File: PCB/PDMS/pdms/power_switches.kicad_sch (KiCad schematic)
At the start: 8 parts

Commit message: PCB clean up
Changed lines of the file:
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@@
-    (stroke (width 0) (type default) (color 0 0 0 0))
-  )
-  (bus_entry (at 213.36 86.36) (size 2.54 -2.54)
     (stroke (width 0) (type default) (color 0 0 0 0))
   )
@@
     (stroke (width 0) (type default) (color 0 0 0 0))
   )
-  (bus_entry (at 213.36 147.32) (size 2.54 -2.54)
+  (bus_entry (at 213.36 153.035) (size 2.54 -2.54)
     (stroke (width 0) (type default) (color 0 0 0 0))
   )
@@
     (stroke (width 0) (type default) (color 0 0 0 0))
   )
-  (bus_entry (at 215.9 86.36) (size 2.54 -2.54)
-    (stroke (width 0) (type default) (color 0 0 0 0))
-  )
   (bus_entry (at 48.26 116.84) (size 2.54 -2.54)
     (stroke (width 0) (type default) (color 0 0 0 0))
@@
     (stroke (width 0) (type default) (color 0 0 0 0))
   )
+  (bus_entry (at 213.36 92.075) (size 2.54 -2.54)
+    (stroke (width 0) (type default) (color 0 0 0 0))
+  )
   (bus_entry (at 185.42 121.92) (size 2.54 2.54)
     (stroke (width 0) (type default) (color 0 0 0 0))
@@
     (stroke (width 0) (type default) (color 0 0 0 0))
   )
-  (bus_entry (at 210.82 147.32) (size 2.54 -2.54)
-    (stroke (width 0) (type default) (color 0 0 0 0))
-  )
-  (bus_entry (at 210.82 86.36) (size 2.54 -2.54)
+  (bus_entry (at 210.82 153.035) (size 2.54 -2.54)
     (stroke (width 0) (type default) (color 0 0 0 0))
   )
@@
     (stroke (width 0) (type default) (color 0 0 0 0))
   )
-  (bus_entry (at 215.9 147.32) (size 2.54 -2.54)
+  (bus_entry (at 210.82 92.075) (size 2.54 -2.54)
+    (stroke (width 0) (type default) (color 0 0 0 0))
+  )
+  (bus_entry (at 215.9 92.075) (size 2.54 -2.54)
+    (stroke (width 0) (type default) (color 0 0 0 0))
+  )
+  (bus_entry (at 215.9 153.035) (size 2.54 -2.54)
     (stroke (width 0) (type default) (color 0 0 0 0))
   )
@@
     (stroke (width 0) (type default) (color 0 0 0 0))
   )
-  (bus (pts (xy 205.74 149.86) (xy 205.74 147.32))
+  (bus (pts (xy 205.74 155.575) (xy 205.74 153.035))
     (stroke (width 0) (type default) (color 0 0 0 0))
   )
@@
     (stroke (width 0) (type default) (color 0 0 0 0))
   )
+  (bus (pts (xy 210.82 92.075) (xy 213.36 92.075))
+    (stroke (width 0) (type default) (color 0 0 0 0))
+  )
   (wire (pts (xy 88.9 68.58) (xy 90.805 68.58))
     (stroke (width 0) (type default) (color 0 0 0 0))
@@
     (stroke (width 0) (type default) (color 0 0 0 0))
   )
-  (bus (pts (xy 213.36 147.32) (xy 215.9 147.32))
-    (stroke (width 0) (type default) (color 0 0 0 0))
-  )
-  (wire (pts (xy 218.44 78.74) (xy 218.44 83.82))
+  (bus (pts (xy 213.36 153.035) (xy 215.9 153.035))
     (stroke (width 0) (type default) (color 0 0 0 0))
   )
@@
     (stroke (width 0) (type default) (color 0 0 0 0))
   )
+  (wire (pts (xy 218.44 78.74) (xy 218.44 89.535))
+    (stroke (width 0) (type default) (color 0 0 0 0))
+  )
   (bus (pts (xy 114.3 88.9) (xy 114.3 111.76))
     (stroke (width 0) (type default) (color 0 0 0 0))
@@
     (stroke (width 0) (type default) (color 0 0 0 0))
   )
-  (bus (pts (xy 210.82 147.32) (xy 213.36 147.32))
+  (bus (pts (xy 210.82 153.035) (xy 213.36 153.035))
     (stroke (width 0) (type default) (color 0 0 0 0))
   )
@@
     (stroke (width 0) (type default) (color 0 0 0 0))
   )
-  (wire (pts (xy 218.44 139.7) (xy 218.44 144.78))
+  (wire (pts (xy 218.44 139.7) (xy 218.44 150.495))
     (stroke (width 0) (type default) (color 0 0 0 0))
   )
@@
     (stroke (width 0) (type default) (color 0 0 0 0))
   )
-  (wire (pts (xy 213.36 78.74) (xy 213.36 83.82))
+  (wire (pts (xy 215.9 78.74) (xy 215.9 89.535))
     (stroke (width 0) (type default) (color 0 0 0 0))
   )
@@
     (stroke (width 0) (type default) (color 0 0 0 0))
   )
-  (bus (pts (xy 215.9 86.36) (xy 218.44 86.36))
-    (stroke (width 0) (type default) (color 0 0 0 0))
-  )
   (bus (pts (xy 185.42 60.96) (xy 185.42 63.5))
     (stroke (width 0) (type default) (color 0 0 0 0))
@@
     (stroke (width 0) (type default) (color 0 0 0 0))
   )
-  (wire (pts (xy 213.36 139.7) (xy 213.36 144.78))
+  (wire (pts (xy 213.36 139.7) (xy 213.36 150.495))
     (stroke (width 0) (type default) (color 0 0 0 0))
   )
@@
     (stroke (width 0) (type default) (color 0 0 0 0))
   )
+  (wire (pts (xy 213.36 78.74) (xy 213.36 89.535))
+    (stroke (width 0) (type default) (color 0 0 0 0))
+  )
   (wire (pts (xy 116.84 66.04) (xy 127 66.04))
     (stroke (width 0) (type default) (color 0 0 0 0))
@@
     (stroke (width 0) (type default) (color 0 0 0 0))
   )
-  (wire (pts (xy 215.9 78.74) (xy 215.9 83.82))
-    (stroke (width 0) (type default) (color 0 0 0 0))
-  )
   (wire (pts (xy 187.96 60.96) (xy 203.2 60.96))
     (stroke (width 0) (type default) (color 0 0 0 0))
@@
     (stroke (width 0) (type default) (color 0 0 0 0))
   )
-  (bus (pts (xy 205.74 88.9) (xy 205.74 86.36))
-    (stroke (width 0) (type default) (color 0 0 0 0))
-  )
   (bus (pts (xy 109.22 73.66) (xy 109.22 93.98))
     (stroke (width 0) (type default) (color 0 0 0 0))
@@
     (stroke (width 0) (type default) (color 0 0 0 0))
   )
+  (bus (pts (xy 205.74 94.615) (xy 205.74 92.075))
+    (stroke (width 0) (type default) (color 0 0 0 0))
+  )
   (wire (pts (xy 111.76 71.12) (xy 127 71.12))
     (stroke (width 0) (type default) (color 0 0 0 0))
   )
-  (bus (pts (xy 213.36 86.36) (xy 215.9 86.36))
-    (stroke (width 0) (type default) (color 0 0 0 0))
-  )
   (bus (pts (xy 43.18 45.72) (xy 53.34 45.72))
     (stroke (width 0) (type default) (color 0 0 0 0))
@@
     (stroke (width 0) (type default) (color 0 0 0 0))
   )
+  (bus (pts (xy 215.9 92.075) (xy 218.44 92.075))
+    (stroke (width 0) (type default) (color 0 0 0 0))
+  )
   (wire (pts (xy 152.4 68.58) (xy 154.305 68.58))
     (stroke (width 0) (type default) (color 0 0 0 0))
@@
     (stroke (width 0) (type default) (color 0 0 0 0))
   )
-  (bus (pts (xy 205.74 86.36) (xy 210.82 86.36))
-    (stroke (width 0) (type default) (color 0 0 0 0))
-  )
-  (wire (pts (xy 215.9 139.7) (xy 215.9 144.78))
-    (stroke (width 0) (type default) (color 0 0 0 0))
-  )
-  (bus (pts (xy 215.9 147.32) (xy 218.44 147.32))
+  (wire (pts (xy 215.9 139.7) (xy 215.9 150.495))
+    (stroke (width 0) (type default) (color 0 0 0 0))
+  )
+  (bus (pts (xy 215.9 153.035) (xy 218.44 153.035))
     (stroke (width 0) (type default) (color 0 0 0 0))
   )
@@
     (stroke (width 0) (type default) (color 0 0 0 0))
   )
-  (bus (pts (xy 205.74 147.32) (xy 210.82 147.32))
+  (bus (pts (xy 205.74 153.035) (xy 210.82 153.035))
     (stroke (width 0) (type default) (color 0 0 0 0))
   )
@@
     (stroke (width 0) (type default) (color 0 0 0 0))
   )
-  (bus (pts (xy 210.82 86.36) (xy 213.36 86.36))
+  (bus (pts (xy 205.74 92.075) (xy 210.82 92.075))
+    (stroke (width 0) (type default) (color 0 0 0 0))
+  )
+  (bus (pts (xy 213.36 92.075) (xy 215.9 92.075))
     (stroke (width 0) (type default) (color 0 0 0 0))
   )
@@
     (stroke (width 0) (type default) (color 0 0 0 0))
   )
+  (label "SPI3_SCK" (at 213.36 88.9 90)
+    (effects (font (size 1.27 1.27)) (justify left bottom))
+  )
   (label "SENS_OUT3" (at 55.88 114.3 0)
     (effects (font (size 1.27 1.27)) (justify left bottom))
@@
     (effects (font (size 1.27 1.27)) (justify left bottom))
   )
-  (label "MISO" (at 218.44 83.82 90)
-    (effects (font (size 1.27 1.27)) (justify left bottom))
-  )
   (label "LP_SIG_IN4" (at 190.5 66.04 0)
     (effects (font (size 1.27 1.27)) (justify left bottom))
@@
     (effects (font (size 1.27 1.27)) (justify left bottom))
   )
-  (label "MOSI" (at 215.9 144.78 90)
+  (label "SPI3_MOSI" (at 215.9 149.86 90)
     (effects (font (size 1.27 1.27)) (justify left bottom))
   )
@@
     (effects (font (size 1.27 1.27)) (justify left bottom))
   )
-  (label "MOSI" (at 215.9 83.82 90)
-    (effects (font (size 1.27 1.27)) (justify left bottom))
-  )
-  (label "SCK" (at 213.36 144.78 90)
-    (effects (font (size 1.27 1.27)) (justify left bottom))
-  )
-  (label "MISO" (at 218.44 144.78 90)
+  (label "SPI3_SCK" (at 213.36 149.86 90)
+    (effects (font (size 1.27 1.27)) (justify left bottom))
+  )
+  (label "SPI3_MISO" (at 218.44 149.86 90)
     (effects (font (size 1.27 1.27)) (justify left bottom))
   )
@@
     (effects (font (size 1.27 1.27)) (justify left bottom))
   )
+  (label "SPI3_MISO" (at 218.44 88.9 90)
+    (effects (font (size 1.27 1.27)) (justify left bottom))
+  )
   (label "LP_SIG_IN6" (at 190.5 121.92 0)
     (effects (font (size 1.27 1.27)) (justify left bottom))
@@
     (effects (font (size 1.27 1.27)) (justify left bottom))
   )
-  (label "SCK" (at 213.36 83.82 90)
+  (label "SPI3_MOSI" (at 215.9 88.9 90)
     (effects (font (size 1.27 1.27)) (justify left bottom))
   )
@@
     )
   )
+  (global_label "{SPI3}" (shape input) (at 205.74 94.615 270) (fields_autoplaced)
+    (effects (font (size 1.27 1.27)) (justify right))
+    (property "Intersheet References" "${INTERSHEET_REFS}" (id 0) (at 205.6606 103.0152 90)
+      (effects (font (size 1.27 1.27)) (justify right) hide)
+    )
+  )
   (global_label "LP_MOS1" (shape input) (at 237.49 53.34 0) (fields_autoplaced)
     (effects (font (size 1.27 1.27)) (justify left))
@@
     )
   )
-  (global_label "{SPI2}" (shape input) (at 205.74 149.86 270) (fields_autoplaced)
-    (effects (font (size 1.27 1.27)) (justify right))
-    (property "Intersheet References" "${INTERSHEET_REFS}" (id 0) (at 205.6606 158.2602 90)
+  (global_label "{SPI3}" (shape input) (at 205.74 155.575 270) (fields_autoplaced)
+    (effects (font (size 1.27 1.27)) (justify right))
+    (property "Intersheet References" "${INTERSHEET_REFS}" (id 0) (at 205.6606 163.9752 90)
       (effects (font (size 1.27 1.27)) (justify right) hide)
     )
@@
     )
   )
-  (global_label "{SPI2}" (shape input) (at 205.74 88.9 270) (fields_autoplaced)
-    (effects (font (size 1.27 1.27)) (justify right))
-    (property "Intersheet References" "${INTERSHEET_REFS}" (id 0) (at 205.6606 97.3002 90)
-      (effects (font (size 1.27 1.27)) (justify right) hide)
-    )
-  )

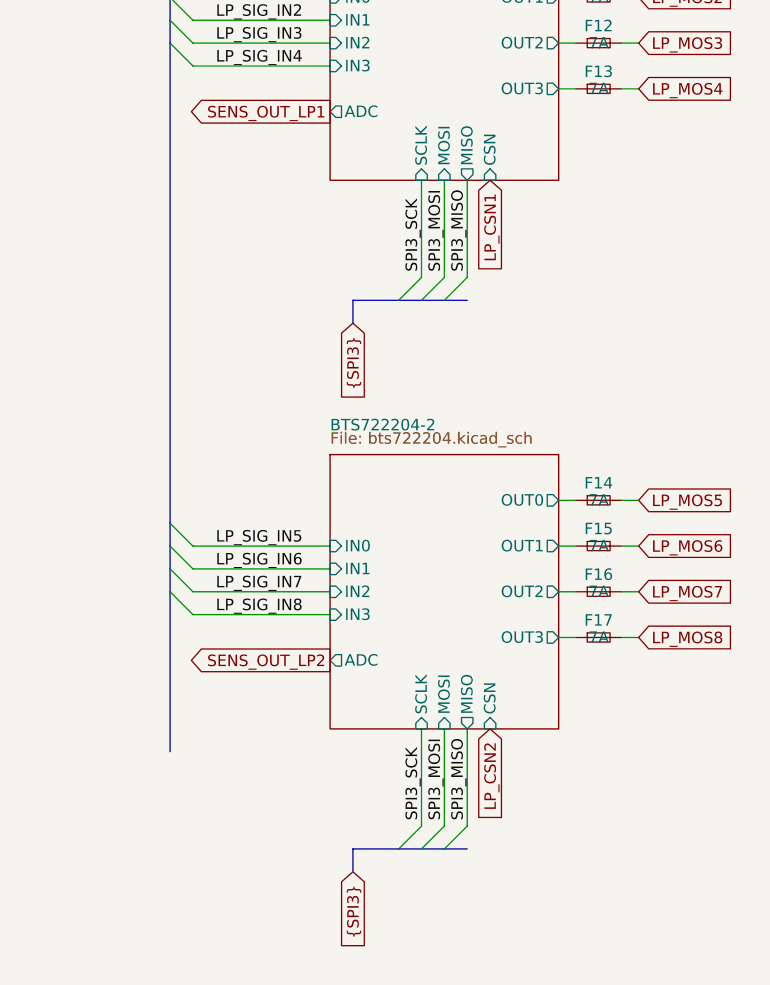
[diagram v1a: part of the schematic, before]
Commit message: Added BLE module
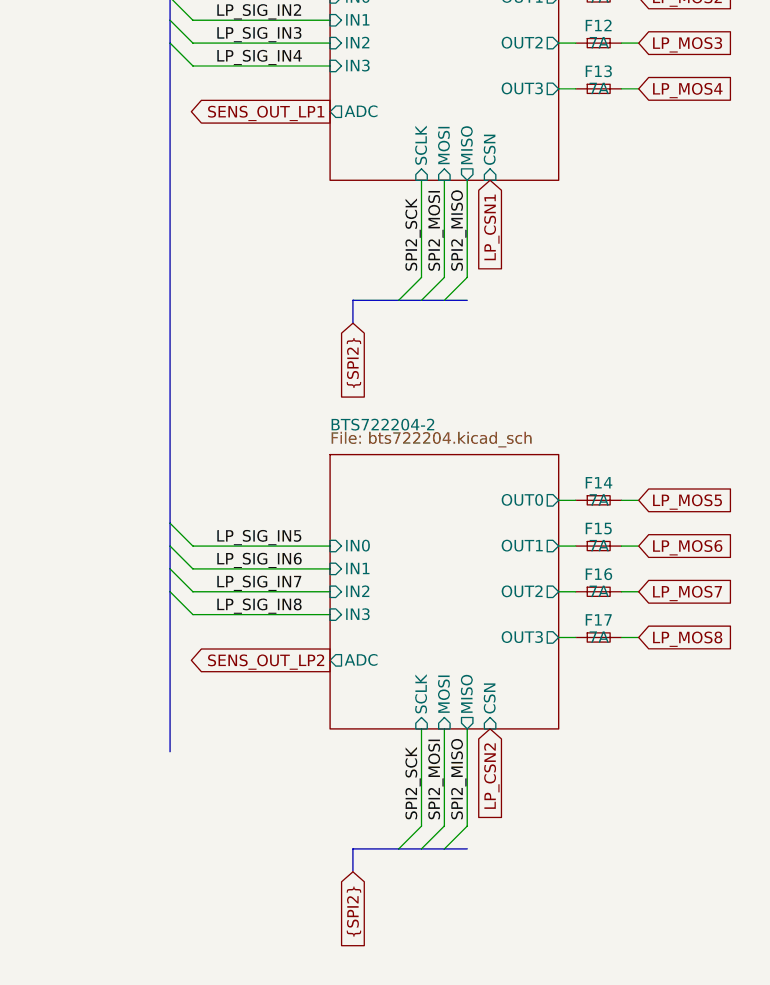
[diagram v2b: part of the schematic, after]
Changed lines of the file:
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@@
     (stroke (width 0) (type default) (color 0 0 0 0))
   )
-  (label "SPI3_SCK" (at 213.36 88.9 90)
+  (label "SPI2_SCK" (at 213.36 88.9 90)
     (effects (font (size 1.27 1.27)) (justify left bottom))
   )
@@
     (effects (font (size 1.27 1.27)) (justify left bottom))
   )
-  (label "SPI3_MOSI" (at 215.9 149.86 90)
+  (label "SPI2_MOSI" (at 215.9 149.86 90)
     (effects (font (size 1.27 1.27)) (justify left bottom))
   )
@@
     (effects (font (size 1.27 1.27)) (justify left bottom))
   )
-  (label "SPI3_SCK" (at 213.36 149.86 90)
-    (effects (font (size 1.27 1.27)) (justify left bottom))
-  )
-  (label "SPI3_MISO" (at 218.44 149.86 90)
+  (label "SPI2_SCK" (at 213.36 149.86 90)
+    (effects (font (size 1.27 1.27)) (justify left bottom))
+  )
+  (label "SPI2_MISO" (at 218.44 149.86 90)
     (effects (font (size 1.27 1.27)) (justify left bottom))
   )
@@
     (effects (font (size 1.27 1.27)) (justify left bottom))
   )
-  (label "SPI3_MISO" (at 218.44 88.9 90)
+  (label "SPI2_MISO" (at 218.44 88.9 90)
     (effects (font (size 1.27 1.27)) (justify left bottom))
   )
@@
     (effects (font (size 1.27 1.27)) (justify left bottom))
   )
-  (label "SPI3_MOSI" (at 215.9 88.9 90)
+  (label "SPI2_MOSI" (at 215.9 88.9 90)
     (effects (font (size 1.27 1.27)) (justify left bottom))
   )
@@
     )
   )
-  (global_label "{SPI3}" (shape input) (at 205.74 94.615 270) (fields_autoplaced)
+  (global_label "{SPI2}" (shape input) (at 205.74 94.615 270) (fields_autoplaced)
     (effects (font (size 1.27 1.27)) (justify right))
     (property "Intersheet References" "${INTERSHEET_REFS}" (id 0) (at 205.6606 103.0152 90)
@@
     )
   )
-  (global_label "{SPI3}" (shape input) (at 205.74 155.575 270) (fields_autoplaced)
+  (global_label "{SPI2}" (shape input) (at 205.74 155.575 270) (fields_autoplaced)
     (effects (font (size 1.27 1.27)) (justify right))
     (property "Intersheet References" "${INTERSHEET_REFS}" (id 0) (at 205.6606 163.9752 90)

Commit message: Major changes with new switch
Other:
- removed sheet BTS50010-1TAE
- removed sheet BTS50010-1TAE1
- removed sheet BTS50010-1TAE2
- removed sheet BTS50010-1TAE3
- removed sheet BTS50010-1TAE4
- removed sheet BTS50010-1TAE5
- removed sheet BTS50010-1TAE6
- removed sheet BTS50010-1TAE7

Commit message: Clean-up of schematics
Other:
- note added: "Low current - power channels - BTS72220"
- moved on the sheet: F10, F11, F12, F13, F14, F15, F16, F17

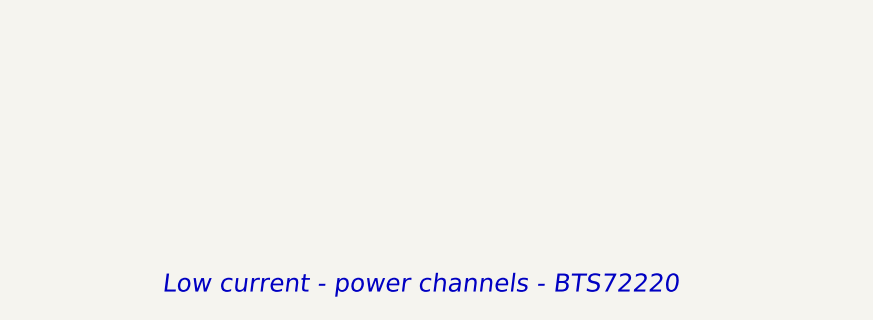
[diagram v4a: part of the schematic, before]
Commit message: WIP PCB folder structure and schematic clean-up
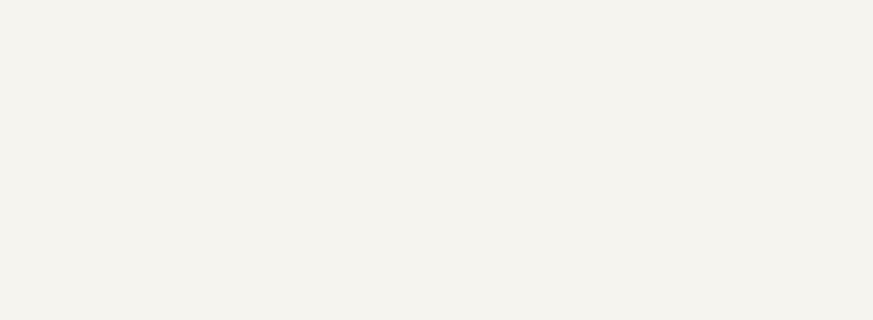
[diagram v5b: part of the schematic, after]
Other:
- note removed: "Low current - power channels - BTS72220"
- company: (none) -> PGRacing Team
- title: (none) -> Low current - power channels - BTS72220
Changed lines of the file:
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@@
 (kicad_sch (version 20211123) (generator eeschema)
   (paper "A4")
+  (title_block
+    (title "Low current - power channels - BTS72220")
+    (rev "V4.2")
+    (company "PGRacing Team")
+    (comment 1 "Karol Pergoł")
+  )
   (bus_entry (at 114.808 114.554) (size 2.54 2.54)
     (stroke (width 0) (type default) (color 0 0 0 0))
@@
     (stroke (width 0) (type default) (color 0 0 0 0))
   )
-  (text "Low current - power channels - BTS72220" (at 186.944 191.008 0)
-    (effects (font (size 2 2) italic) (justify left bottom))
-  )
   (label "SPI2_SCK" (at 142.748 84.074 90)
